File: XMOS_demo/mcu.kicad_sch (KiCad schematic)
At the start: 45 parts, among them J1 XSYS2 DEBUG CONNECTOR, U1 U316-1024-QF60B, U2 W25Q32JVSS, Y1 Crystal_24M

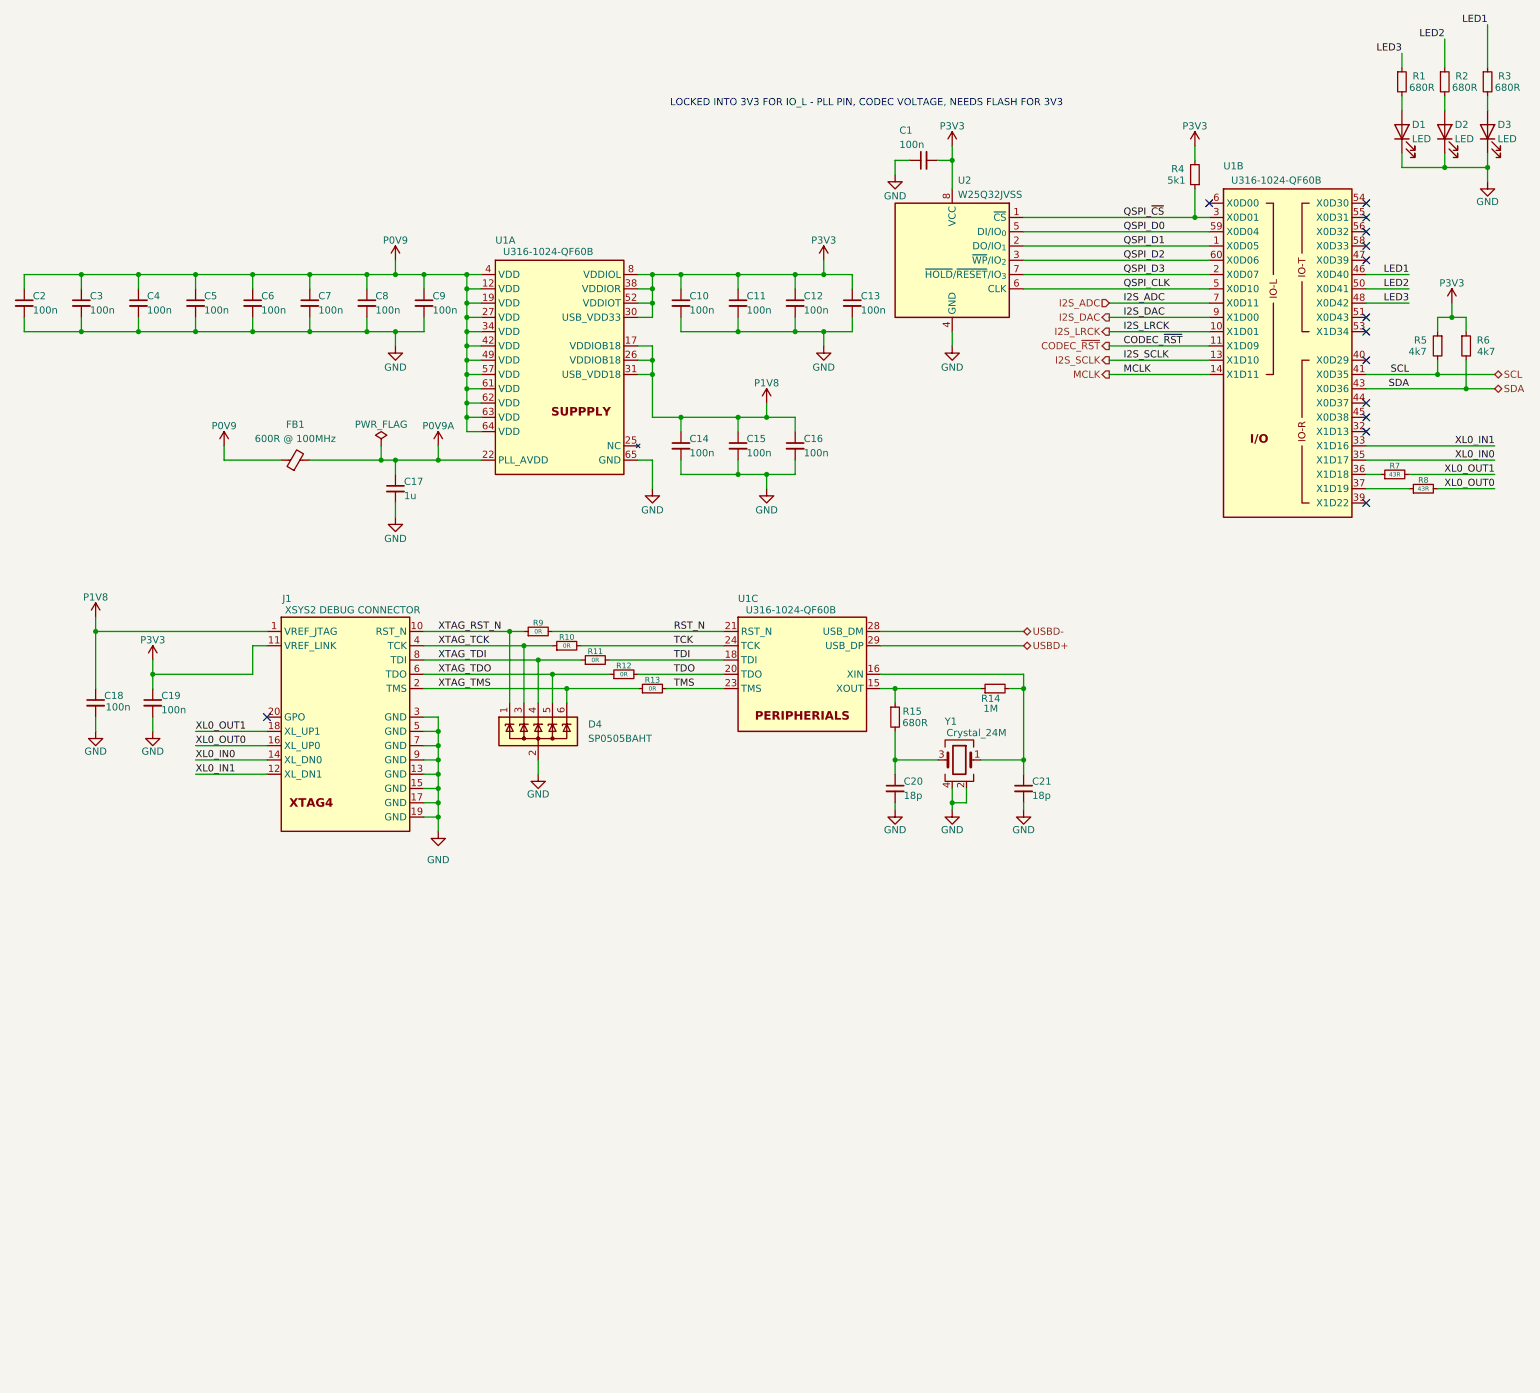
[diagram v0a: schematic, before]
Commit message: PCB work, changes for better routing
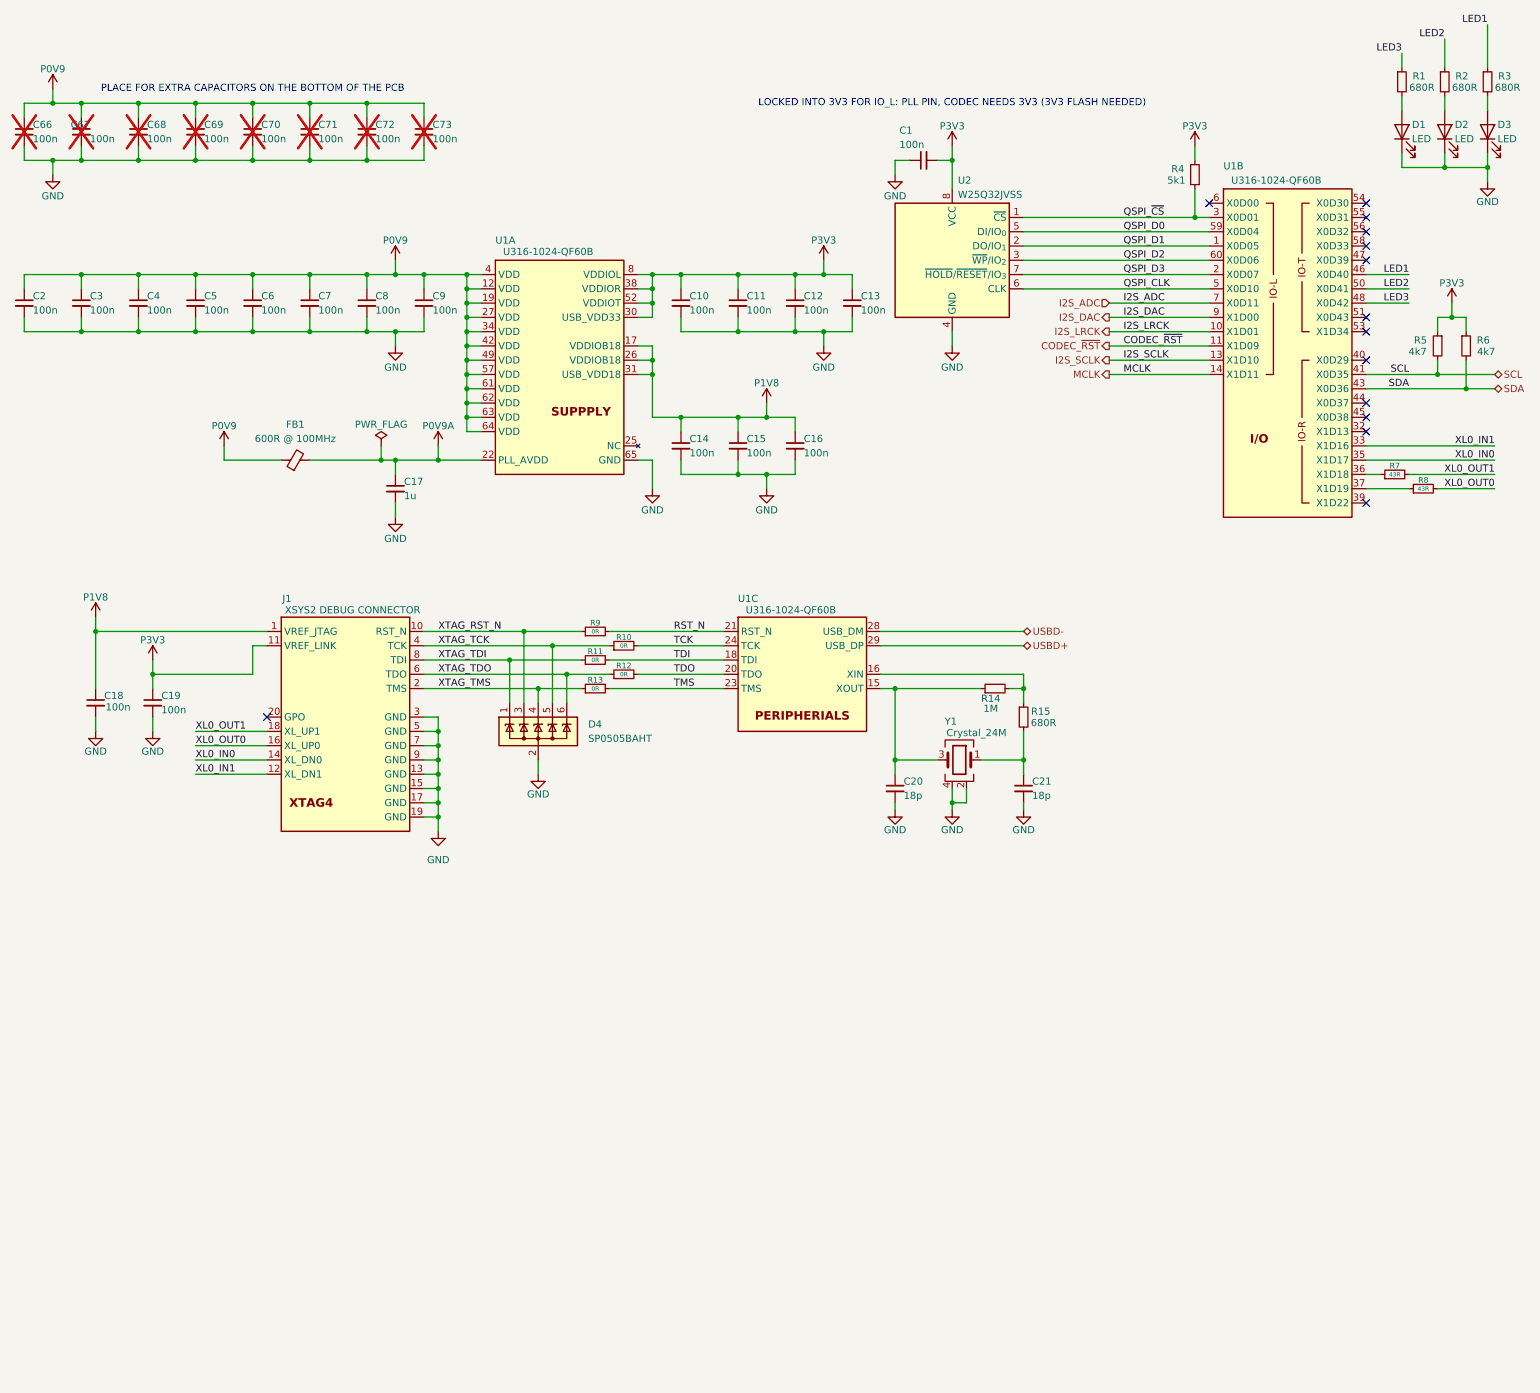
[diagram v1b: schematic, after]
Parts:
- added C66, C67, C68, C69, C70, C71, C72, C73: 100n, Capacitor_SMD:C_0402_1005Metric, symbol Device:C_Small
- C20, C21: footprint Capacitor_SMD:C_0603_1608Metric -> Capacitor_SMD:C_0402_1005Metric
- R14, R15: footprint Resistor_SMD:R_0603_1608Metric -> Resistor_SMD:R_0402_1005Metric
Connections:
- net GND: now also C66.2, C67.2, C68.2, C69.2, C70.2, C71.2, C72.2, C73.2
- net P0V9: now also C66.1, C67.1, C68.1, C69.1, C70.1, C71.1, C72.1, C73.1
- net XTAG_RST_N: now also D4.3 (K); no longer D4.1 (K)
- net XTAG_TCK: now also D4.5 (K); no longer D4.3 (K)
- net XTAG_TDI: now also D4.1 (K); no longer D4.4 (K)
- net XTAG_TDO: now also D4.6 (K); no longer D4.5 (K)
- net XTAG_TMS: now also D4.4 (K); no longer D4.6 (K)
- net at C20.1, Y1.3: now also R14.1, U1.15 (XOUT); no longer R15.2
- net at R14.2, U1.16 (XIN): now also R15.1; no longer C21.1, Y1.1
- new net: C21.1, R15.2, Y1.1
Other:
- note added: "LOCKED INTO 3V3 FOR IO_L: PLL PIN, CODEC NEEDS 3V3 (3V3 FLASH NEEDED)"
- note added: "PLACE FOR EXTRA CAPACITORS ON THE BOTTOM OF THE PCB"
- note removed: "LOCKED INTO 3V3 FOR IO_L - PLL PIN, CODEC VOLTAGE, NEEDS FLASH FOR 3V3"
- moved on the sheet: R10, R13, R15, R9

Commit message: sch work changes (jumpers, connectors, tp)
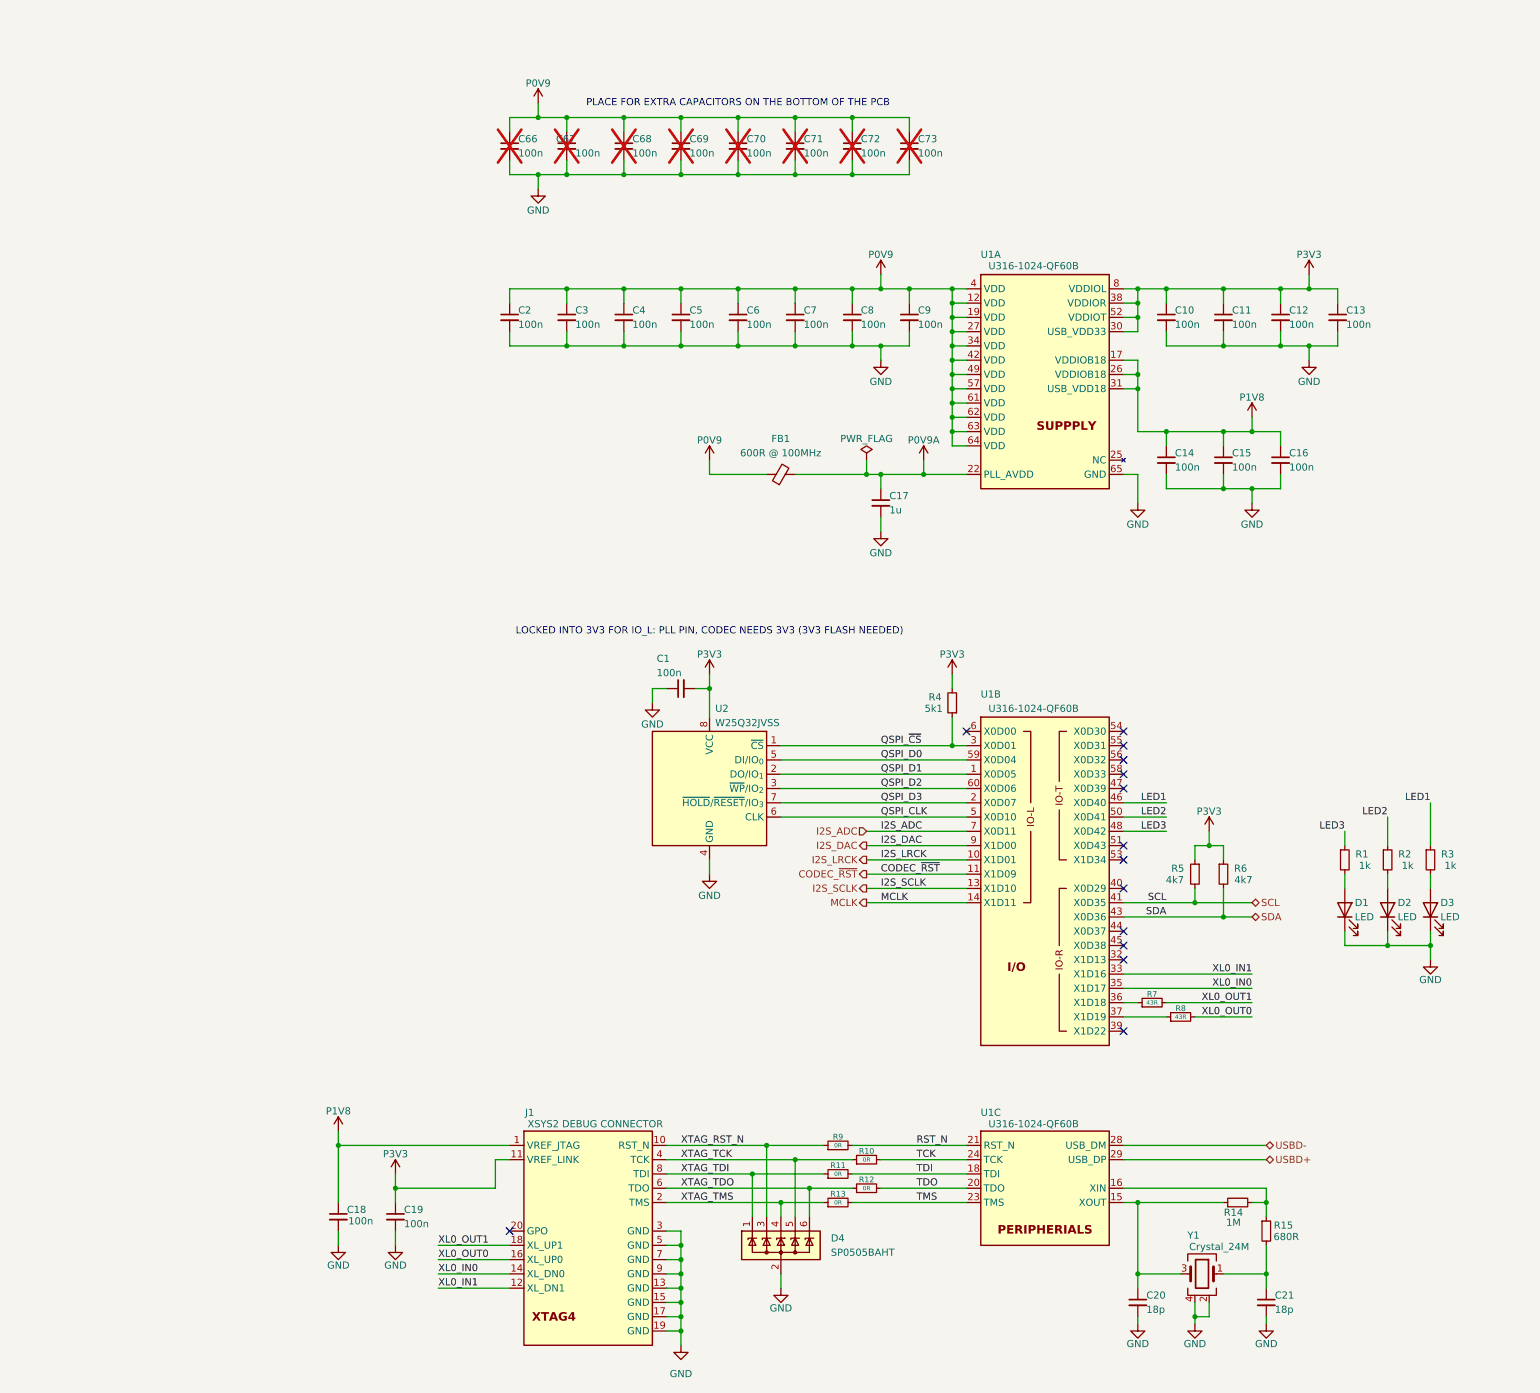
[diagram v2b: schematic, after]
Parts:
- R1, R2, R3: value 680R -> 1k
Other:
- moved on the sheet: C1, C10, C11, C12, C13, C14, C15, C16, C17, C18, C19, C2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

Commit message: merge
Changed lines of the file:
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@@
+	(wire
+		(pts
+			(xy 254 60.96) (xy 261.62 60.96)
+		)
+		(stroke
+			(width 0)
+			(type default)
+		)
+	)
 	(wire
 		(pts

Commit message: pcb routing
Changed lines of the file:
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@@
-	(wire
-		(pts
-			(xy 254 60.96) (xy 261.62 60.96)
-		)
-		(stroke
-			(width 0)
-			(type default)
-		)
-	)
 	(wire
 		(pts

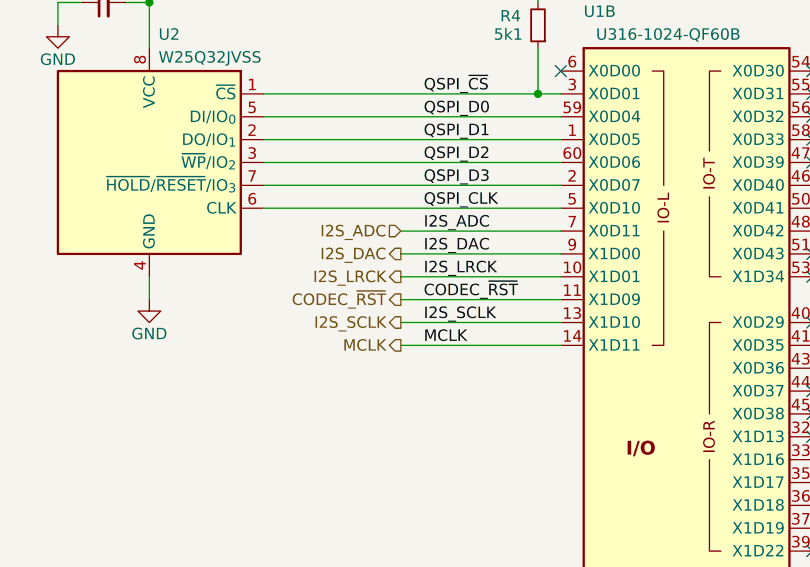
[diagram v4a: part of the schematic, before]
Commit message: I2S config sch page added
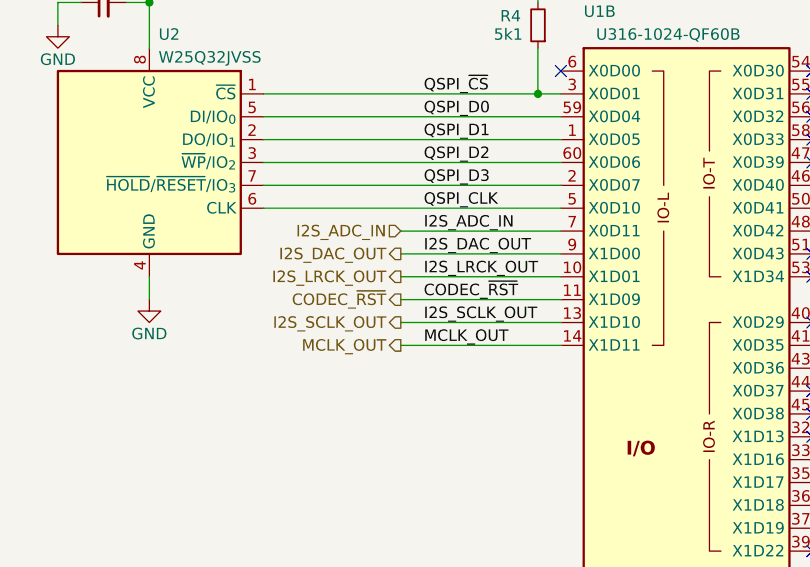
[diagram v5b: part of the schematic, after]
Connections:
- net I2S_ADC renamed I2S_ADC_IN
- net I2S_DAC renamed I2S_DAC_OUT
- net I2S_LRCK renamed I2S_LRCK_OUT
- net I2S_SCLK renamed I2S_SCLK_OUT
- net MCLK renamed MCLK_OUT
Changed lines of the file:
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@@
 		)
 	)
-	(label "MCLK"
+	(label "MCLK_OUT"
 		(at 167.64 172.72 0)
 		(effects
@@
 		)
 	)
-	(label "I2S_SCLK"
+	(label "I2S_SCLK_OUT"
 		(at 167.64 170.18 0)
 		(effects
@@
 		)
 	)
-	(label "I2S_LRCK"
+	(label "I2S_LRCK_OUT"
 		(at 167.64 165.1 0)
 		(effects
@@
 		)
 	)
-	(label "I2S_DAC"
+	(label "I2S_DAC_OUT"
 		(at 167.64 162.56 0)
 		(effects
@@
 		)
 	)
-	(label "I2S_ADC"
+	(label "I2S_ADC_IN"
 		(at 167.64 160.02 0)
 		(effects
@@
 		)
 	)
-	(hierarchical_label "I2S_SCLK"
+	(hierarchical_label "I2S_SCLK_OUT"
 		(shape output)
 		(at 165.1 170.18 180)
@@
 		)
 	)
-	(hierarchical_label "I2S_DAC"
+	(hierarchical_label "I2S_DAC_OUT"
 		(shape output)
 		(at 165.1 162.56 180)
@@
 		)
 	)
-	(hierarchical_label "I2S_LRCK"
+	(hierarchical_label "I2S_LRCK_OUT"
 		(shape output)
 		(at 165.1 165.1 180)
@@
 		)
 	)
-	(hierarchical_label "MCLK"
+	(hierarchical_label "MCLK_OUT"
 		(shape output)
 		(at 165.1 172.72 180)
@@
 		)
 	)
-	(hierarchical_label "I2S_ADC"
+	(hierarchical_label "I2S_ADC_IN"
 		(shape input)
 		(at 165.1 160.02 180)

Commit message: Summary (required)
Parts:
- renumbered C66 to C1, C3 to C10, C4 to C11, C5 to C12, C6 to C13, C7 to C14, C8 to C15, C9 to C16, C10 to C17, C11 to C18, C12 to C19, C67 to C2, C13 to C20, C14 to C21, C15 to C22, C16 to C23, C17 to C24, C1 to C25, C18 to C26, C19 to C27, C20 to C28, C21 to C29, C68 to C3, C69 to C4, C70 to C5, C71 to C6, C72 to C7, C73 to C8, C2 to C9, R5 to R10, R6 to R11, R7 to R12, R8 to R13, R9 to R14, R10 to R15, R11 to R16, R12 to R17, R13 to R18, R14 to R19, R15 to R20, R4 to R6, R1 to R7, R2 to R8, R3 to R9
